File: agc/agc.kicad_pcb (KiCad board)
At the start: 4 copper layers, 72.4 x 99.8 mm, 111 parts, among them J1 SMA_DAC, J2 SMA_LPTR, J3 SMA_DRIVER, J4 SMA_RX, J5 SIL10, J6 SMA_LPTR, K1 TR, K2 TR, K3 VIN, K4 VOUT_TR, K5 TR, K6 TR, K7 HVMON, P10 CONN_2, P2 FWD_FAULT, P3 REF_FAULT, P4 CONN_8X2, P5 COUPLED_TEST, P6 TP_VCC, P7 COUPLED_TEST, P8 COUPLED_TEST, P9 COUPLED_TEST, U1 BA08CC0WFP, U10 74AHC1G04, U11 74AHC1G04, U12 78SRH-5/2-C, U14 SMP1330-005LF, U15 SMP1330-005LF, U16 SMP1330-005LF, U2 HMC475, U3 HMC595, U4 HMC595, U5 HMC595, U6 74AHC1G04, U7 ISL3281E, U9 LTC2914-2

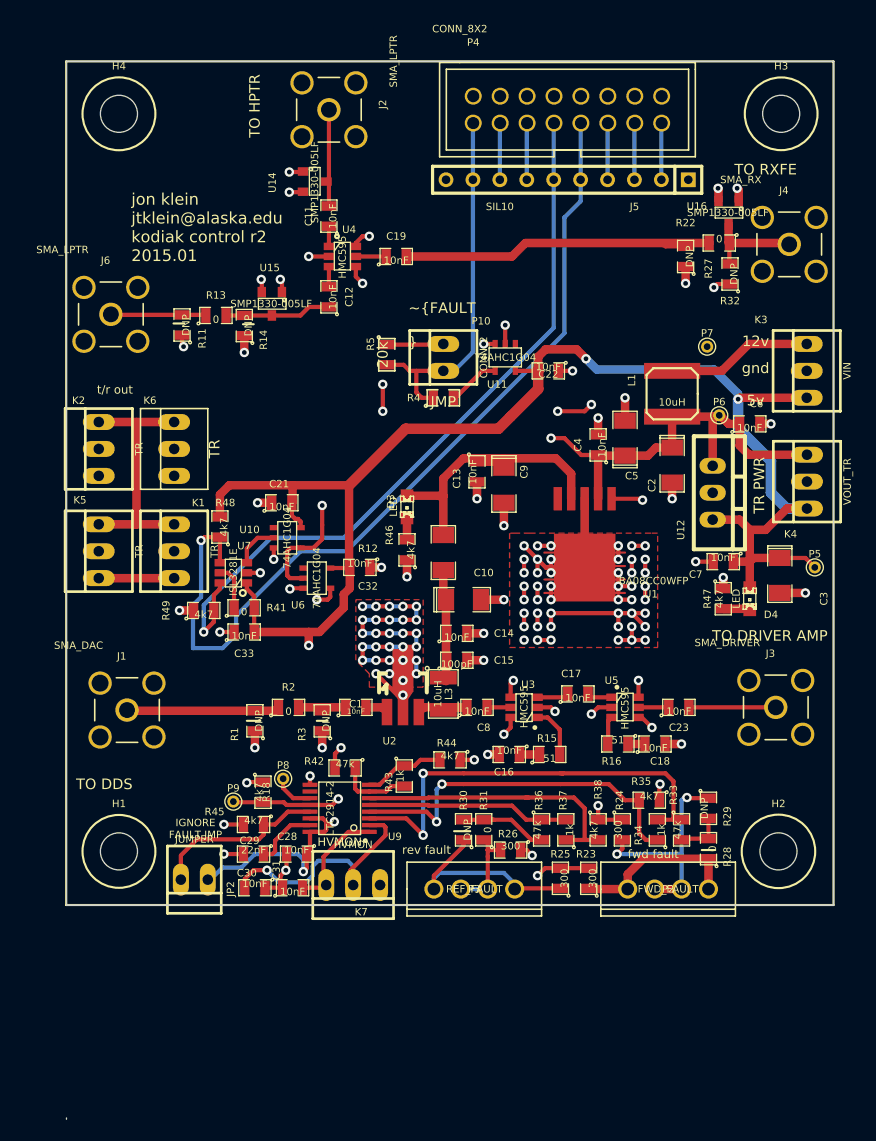
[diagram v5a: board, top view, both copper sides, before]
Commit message: moved rf amps from control board to rxfe and driver
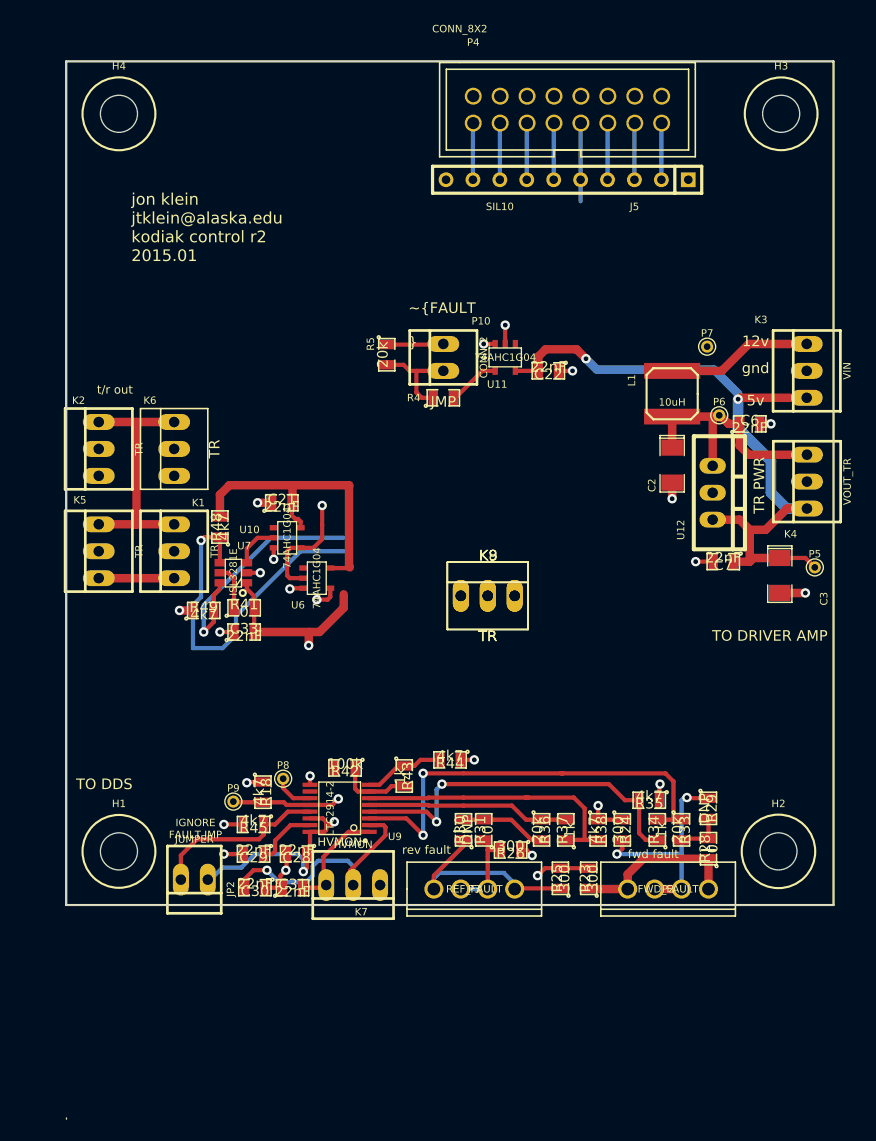
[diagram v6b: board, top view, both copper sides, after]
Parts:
- removed C1: 10nF, SMD_Packages:SMD-0805
- removed C10, C5, C9: 4.7uF, SMD_Packages:SM1206POL
- removed C11, C12, C13, C14, C16, C17, C18, C19, C23, C32, C4, C8: 10nF, SMD_Packages:SM0805
- removed C15: 100pF, SMD_Packages:SM0805
- removed D3, D4: LED, LEDs:LED-0805
- removed J1: SMA_DAC, ocal:SMA_5-1814832-1
- removed J2, J6: SMA_LPTR, ocal:SMA_5-1814832-1
- removed J3: SMA_DRIVER, ocal:SMA_5-1814832-1
- removed J4: SMA_RX, ocal:SMA_5-1814832-1
- removed L3: 10uH, SMD_Packages:SM1210
- removed R1, R11, R14, R22, R3, R32: DNP, SMD_Packages:SM0805
- removed R12: 9.1 (.25W), SMD_Packages:SM1206
- removed R13, R2, R27: 0, SMD_Packages:SM0805
- removed R15, R16: 51, SMD_Packages:SM0805
- removed R46, R47: 4k7, SMD_Packages:SM0805
- removed U1: BA08CC0WFP, to252_5:TO252-5
- removed U14, U15, U16: SMP1330-005LF, SMD_Packages:SOT23
- removed U2: HMC475, Housings_SOT-89:SOT89-3_Housing_Handsoldering
- removed U3, U4, U5: HMC595, SMD_Packages:SOT23_6
- added K8, K9: TR, Connect:PINHEAD1-3, F.Cu at (72.8, 83.5)
- C21, C22, C28, C30, C31, C33, C6, C7: value 10nF -> 22nF; footprint SMD_Packages:SM0805 -> SMD_Packages:SMD-0805
- C29, R18, R23, R24, R25, R26, R28, R29, R30, R31, R34, R35, R37, R38, R41, R43, R44, R45, R48, R49: footprint SMD_Packages:SM0805 -> SMD_Packages:SMD-0805
- R33, R36: value 47k -> 20k; footprint SMD_Packages:SM0805 -> SMD_Packages:SMD-0805
- R42: value 47k -> 100k; footprint SMD_Packages:SM0805 -> SMD_Packages:SMD-0805
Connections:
- R33 pad 2: Net-(R28-Pad2) -> Net-(R30-Pad2)
- R36 pad 2: Net-(R30-Pad2) -> Net-(R28-Pad2)
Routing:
- net GND: track 229.1 -> 39.5 mm, vias 125 -> 20
- net /~TX: track 194.2 -> 78.9 mm, vias 8 -> 1
- net /TX: track 142.1 -> 45.9 mm, vias 4 -> 1
- net VCC: track 85.0 -> 23.8 mm, vias 2 -> 0
- net +5V: track 216.9 -> 174.4 mm
- net /TRB: track 83.6 -> 41.5 mm
- net /TRA: track 71.0 -> 29.0 mm
- net Net-(C19-Pad2): track 33.8 -> 0.00 mm
- net Net-(C13-Pad1): track 29.3 -> 0.00 mm
- net /~FAULT: track 35.1 -> 16.3 mm
- net Net-(C10-Pad1): track 15.8 -> 0.00 mm
- net Net-(J1-Pad1): track 15.7 -> 0.00 mm
- net /FAULT: track 110.8 -> 97.1 mm, vias 3 -> 2
- net Net-(C12-Pad1): track 10.6 -> 0.00 mm
- net Net-(J4-Pad1): track 9.49 -> 0.00 mm
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- removed copper zone on F.Cu, net GND
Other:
- board text removed: "TO HPTR"
- board text removed: "TO RXFE"

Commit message: finished layout on r1 control board - reduced bom variety, eliminated rf, reduced board size
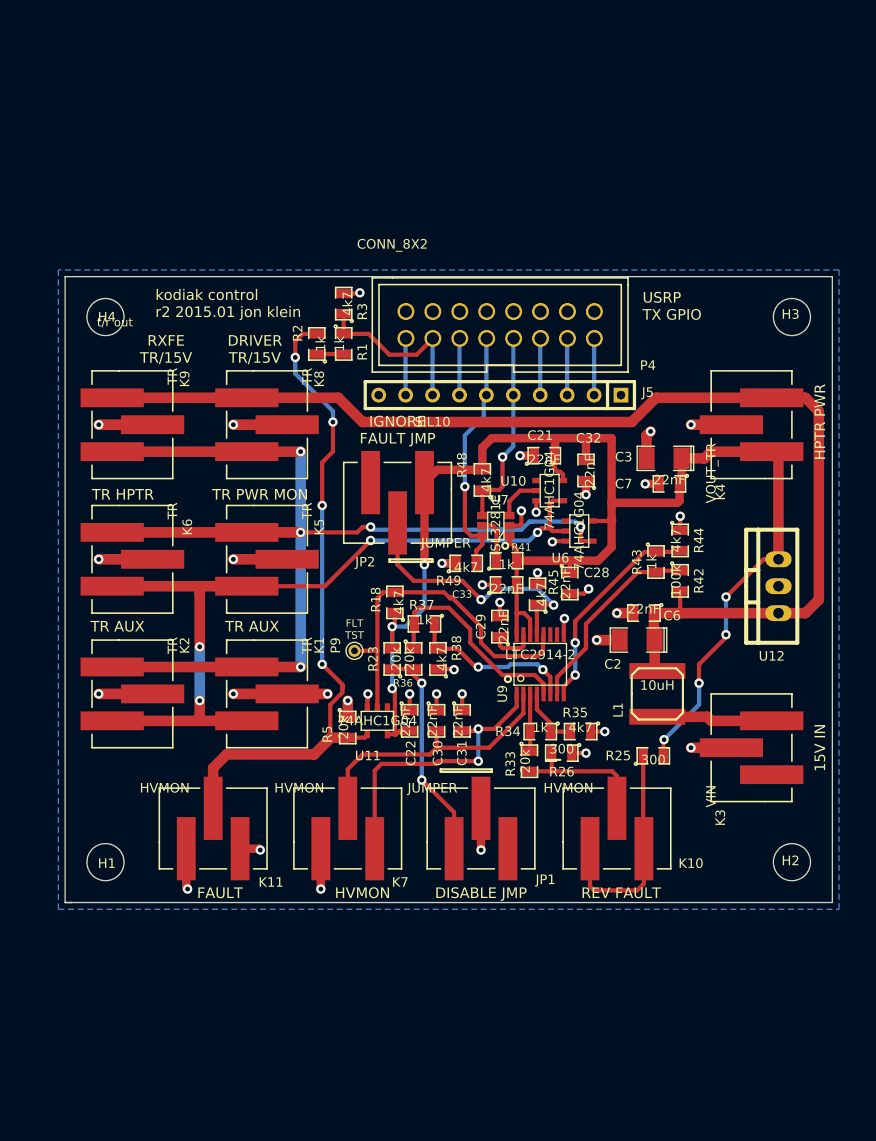
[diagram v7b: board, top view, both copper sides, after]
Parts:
- removed P10: CONN_2, Connect:PINHEAD1-2
- removed P2: FWD_FAULT, localconn:conn4
- removed P3: REF_FAULT, localconn:conn4
- removed P5, P7, P8: COUPLED_TEST, Connect:PINTST
- removed P6: TP_VCC, Connect:PINTST
- removed R24: 300, SMD_Packages:SMD-0805
- removed R28, R31: 0, SMD_Packages:SMD-0805
- removed R29, R30: DNP, SMD_Packages:SMD-0805
- removed R4: JMP, SMD_Packages:SMD-0805
- added C32: 22nF, SMD_Packages:SMD-0805, F.Cu at (82.0, 71.6)
- added JP1: JUMPER, localconn:3-647166-3, F.Cu at (72.1, 105.4)
- added K10: HVMON, localconn:3-647166-3, F.Cu at (85.0, 105.4)
- added K11: HVMON, localconn:3-647166-3, F.Cu at (46.9, 105.4)
- added R1: 1k, SMD_Packages:SMD-0805, F.Cu at (59.2, 59.7)
- added R2: 1k, SMD_Packages:SMD-0805, F.Cu at (56.6, 59.7)
- added R3: 4k7, SMD_Packages:SMD-0805, F.Cu at (59.2, 55.9)
- C2: value 47uF -> 20 uF
- C3: value 4.7uF -> 20 uF
- JP2: footprint Connect:PINHEAD1-2 -> localconn:3-647166-3
- K1, K2, K3, K4, K5, K6, K7, K8, K9: footprint Connect:PINHEAD1-3 -> localconn:3-647166-3
- R23: value 300 -> 20k
- R41: value 0 -> 1k
- moved JP2 40.4 mm to (64.3, 74.7)
- moved K9 37.2 mm to (39.2, 67.3), turned to 270 degrees
- moved U11 36.4 mm to (62.4, 95.2)
- moved C28 36.3 mm to (80.5, 82.3), turned to 270 degrees
- moved R42 36.2 mm to (90.9, 82.0), turned to 270 degrees
- moved K3 35.9 mm to (97.7, 97.8)
- moved C22 35.5 mm to (65.4, 95.2), turned to 270 degrees
- moved R5 35.4 mm to (59.6, 95.9)
- moved R45 34.5 mm to (77.5, 83.3), turned to 90 degrees
- moved C29 31.6 mm to (73.9, 86.4), turned to 90 degrees
- moved R43 31.2 mm to (88.6, 80.3)
- moved R44 30.0 mm to (90.9, 78.2), turned to 270 degrees
- moved L1 28.4 mm to (88.8, 92.7), turned to 90 degrees
- moved R23 27.8 mm to (63.8, 89.4)
- moved K8 26.4 mm to (51.9, 67.3), turned to 270 degrees
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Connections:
- J5 pad 9: /~FAULT -> Net-(J5-Pad9)
- P4 pad 1: /~FAULT -> Net-(J5-Pad9)
- R23 pad 1: Net-(P2-Pad1) -> Net-(JP1-Pad1)
- R26 pad 2: Net-(P3-Pad2) -> Net-(K10-Pad2)
- R33 pad 2: Net-(R30-Pad2) -> Net-(K10-Pad2)
- R36 pad 2: Net-(R28-Pad2) -> Net-(JP1-Pad1)
- U11 pad 4: Net-(R4-Pad2) -> /~FAULT
- U9 pad 11: Net-(P8-Pad1) -> (no net)
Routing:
- net VCC: track 23.8 -> 110.6 mm
- net /FAULT: track 97.1 -> 33.9 mm, vias 2 -> 0
- net /TX: track 45.9 -> 103.6 mm, vias 1 -> 5
- net GND: track 39.5 -> 94.2 mm, vias 20 -> 38
- net /~FAULT: track 16.3 -> 62.8 mm, vias 0 -> 4
- net Net-(R33-Pad1): track 42.4 -> 5.42 mm, vias 2 -> 0
- net (no net): track 0.00 -> 34.9 mm
- net Net-(R34-Pad1): track 34.8 -> 5.98 mm, vias 2 -> 0
- net +5V: track 174.4 -> 148.7 mm
- net /TRB: track 41.5 -> 18.8 mm
- net Net-(P2-Pad2): track 21.2 -> 0.00 mm, vias 2 -> 0
- net Net-(JP1-Pad1): track 0.00 -> 20.6 mm, vias 0 -> 2
- net Net-(C31-Pad2): track 10.7 -> 27.9 mm, vias 0 -> 2
- net Net-(P2-Pad1): track 15.6 -> 0.00 mm
- net Net-(K10-Pad2): track 0.00 -> 13.4 mm
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- added copper zone on B.Cu, net GND
- removed copper zone on TopMid.Cu, net GND
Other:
- board size 72.4 x 99.8 mm -> 72.4 x 59.1 mm
- copper layers 4 -> 2
- board text added: "15V IN"
- board text added: "DISABLE JMP"
- board text added: "DRIVER TR/15V"
- board text added: "FAULT"
- board text added: "FLT TST"
- board text added: "HPTR PWR"
- board text added: "REV FAULT"
- board text added: "RXFE TR/15V"
- board text added: "TR AUX"
- board text added: "TR HPTR"
- board text added: "TR PWR MON"
- board text added: "USRP TX GPIO"
- board text added: "kodiak control r2 2015.01 jon klein"
- board text removed: "12v"
- board text removed: "5v"
- board text removed: "TO DDS"
- board text removed: "TO DRIVER AMP"
- board text removed: "TR PWR"
- board text removed: "fwd fault"
- board text removed: "gnd"
- board text removed: "rev fault"
- board text removed: "~FAULT"

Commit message: added fiducial marker footprint and marks to control board. increased default solderpaste clearance to .05 mm on control
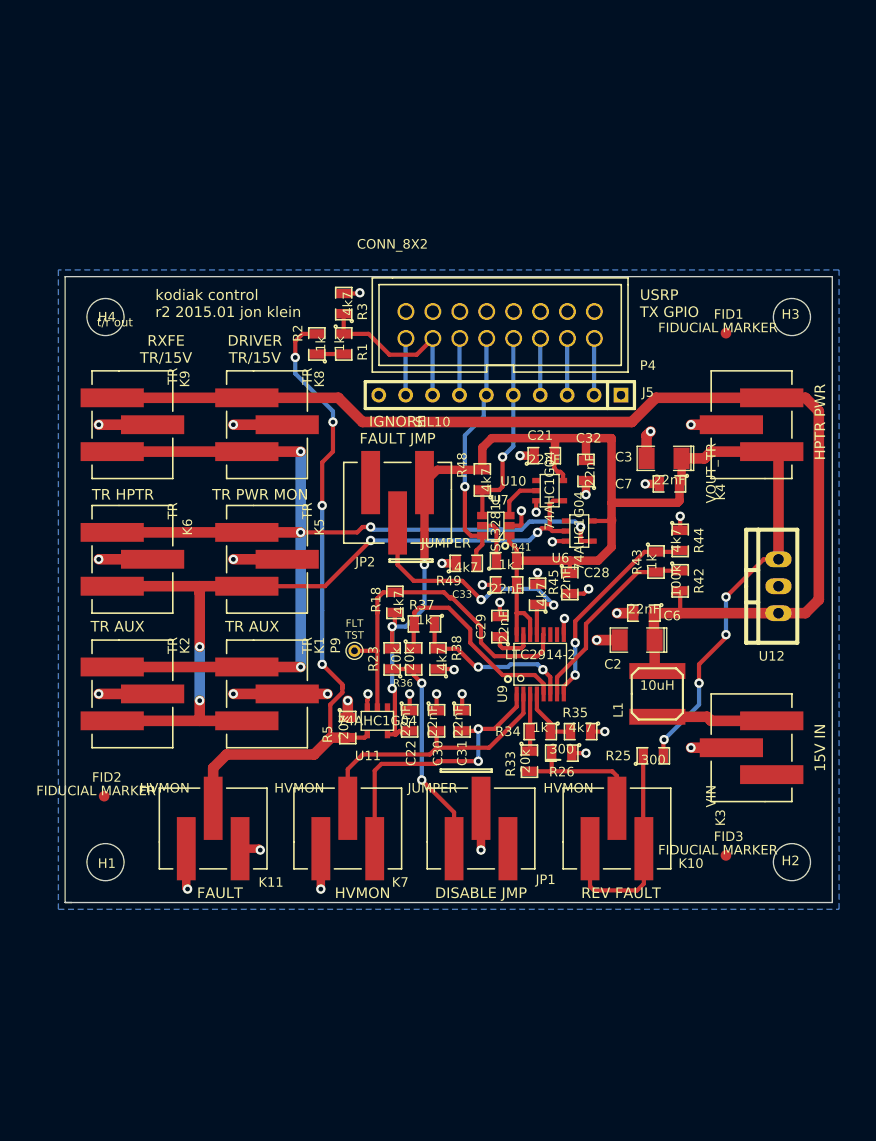
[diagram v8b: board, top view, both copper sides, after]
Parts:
- added FID1: FIDUCIAL MARKER, sdtransmitter:FID_1MM, F.Cu at (95.2, 58.7)
- added FID2: FIDUCIAL MARKER, sdtransmitter:FID_1MM, F.Cu at (36.6, 102.4)
- added FID3: FIDUCIAL MARKER, sdtransmitter:FID_1MM, F.Cu at (95.2, 108.0)
